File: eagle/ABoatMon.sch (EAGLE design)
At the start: 29 parts, among them J1 5V, J2 GND, J3 GND, J4 5V, X1 MKDSN1,5/2-5,08

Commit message: added M0
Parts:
- removed C1: 0.1U, SparkFun-Capacitors:0.1UF-KIT-EZ-50V-20%
- removed J4: 5V, SparkFun-Connectors:CONN_01
- removed JST1: LIPO, adafruit:JST_2PIN-THM
- removed LIPO: (no value), microbuilder:HEADER-1X2ROUND
- removed MOTEINO_MEGA: HEADERS, Moteino:MOTEINO_MEGA_SIMPLE
- removed R2: 1.8M, SparkFun-Resistors:1KOHM-HORIZ-1/4W-1%
- removed R3: 3.3M, SparkFun-Resistors:1KOHM-HORIZ-1/4W-1%
- added U$6: MOTEINO_M0, Moteino:MOTEINO_M0
- J1: value 5V -> VUSB
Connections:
- removed net 5V: J1.1, J4.1
- removed net A0: C1.1, MOTEINO_MEGA.A0, R2.1, R3.2
- removed net A5_VCC_VD: C2.1, MOTEINO_MEGA.A5, R5.2, R6.1
- removed net D10_GPS_RX: JP1.5, MOTEINO_MEGA.D10_RX1
- removed net D11_GPS_TX: JP1.4, MOTEINO_MEGA.D11_TX1
- removed net D12_GPS_ENABLE: JP1.8, MOTEINO_MEGA.D12
- removed net D13_FONA_NETSTAT: FONA.2, MOTEINO_MEGA.D13
- removed net D14_FONA_KEY: FONA.6, MOTEINO_MEGA.D14
- removed net D18_FONA_PS: FONA.7, MOTEINO_MEGA.D18
- removed net D19_PWRON: ENABLE.1, MOTEINO_MEGA.D19
- removed net D25_LED_SWITCH: JST.6, MOTEINO_MEGA.A1
- removed net D26_LED: MOTEINO_MEGA.A2, R7.2
- removed net D27_DS_PWR: JST.3, MOTEINO_MEGA.A3, R1.1
- removed net D28_DS_DATA: JST.5, MOTEINO_MEGA.A4, R1.2
- removed net D8_FONA_TX: FONA.3, MOTEINO_MEGA.D8_RX0
- removed net D9_FONA_RX: FONA.4, MOTEINO_MEGA.D9_TX0
- removed net VIN: FONA.12, LIPO.1, MOTEINO_MEGA.VIN, MOTEINO_MEGA.VIN_2, R2.2
- removed net VIN_JUMPER: JST1.2, LIPO.2
- new net A1_VCC_VD: C2.1, R5.2, R6.1, U$6.A1
- new net D0_RX_GPS: JP1.5, U$6.D0_RX1
- new net D10_FONA_KEY: FONA.6, U$6.D10
- new net D11_FONA_PS: FONA.7, U$6.D11
- new net D12_PWRON: ENABLE.1, U$6.D12
- new net D1_TX_GPS: JP1.4, U$6.D1_TX1
- new net D30_TX_FONA: FONA.3, U$6.D30_TX
- new net D31_RX_FONA: FONA.4, U$6.D31_RX
- new net D4_LED: R7.2, U$6.D4
- new net D5_LED_SWITCH: JST.6, U$6.D5
- new net D6_DS_PWR: JST.3, R1.1, U$6.D6
- new net D7_DS_DATA: JST.5, R1.2, U$6.D7
- new net D8_FONA_NETSTAT: FONA.2, U$6.D8
- new net D9_GPS_ENABLE: JP1.8, U$6.D9_DIO0
- new net VUSB: FONA.12, J1.1, U$6.VUSB
- net 3.3V: now also U$6.3V3, U$6.3V3_2; no longer MOTEINO_MEGA.3V3, MOTEINO_MEGA.3V3_2
- net D3_BILGESW: now also U$6.D3; no longer MOTEINO_MEGA.D3
- net GND: now also U$6.GND, U$6.GND1, U$6.GND2; no longer C1.2, JST1.1, MOTEINO_MEGA.GND1, MOTEINO_MEGA.GND2, R3.1
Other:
- note removed: "LIPO Voltage Divider/ADC"
- moved on the sheet: JP1, R1

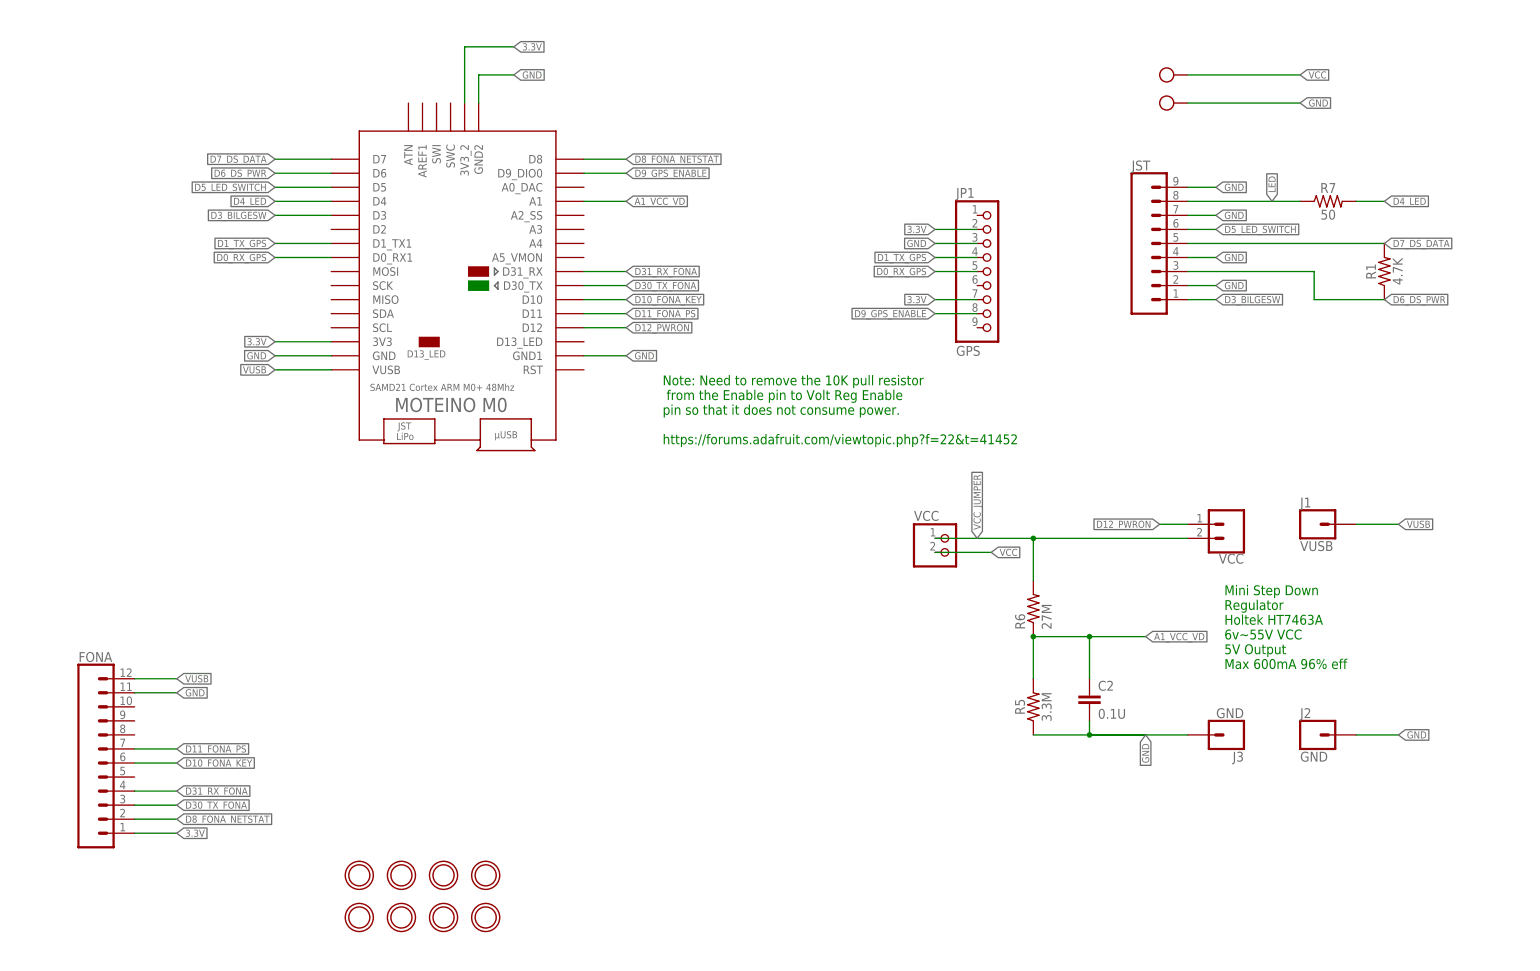
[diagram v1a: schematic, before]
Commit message: added CAM-M8
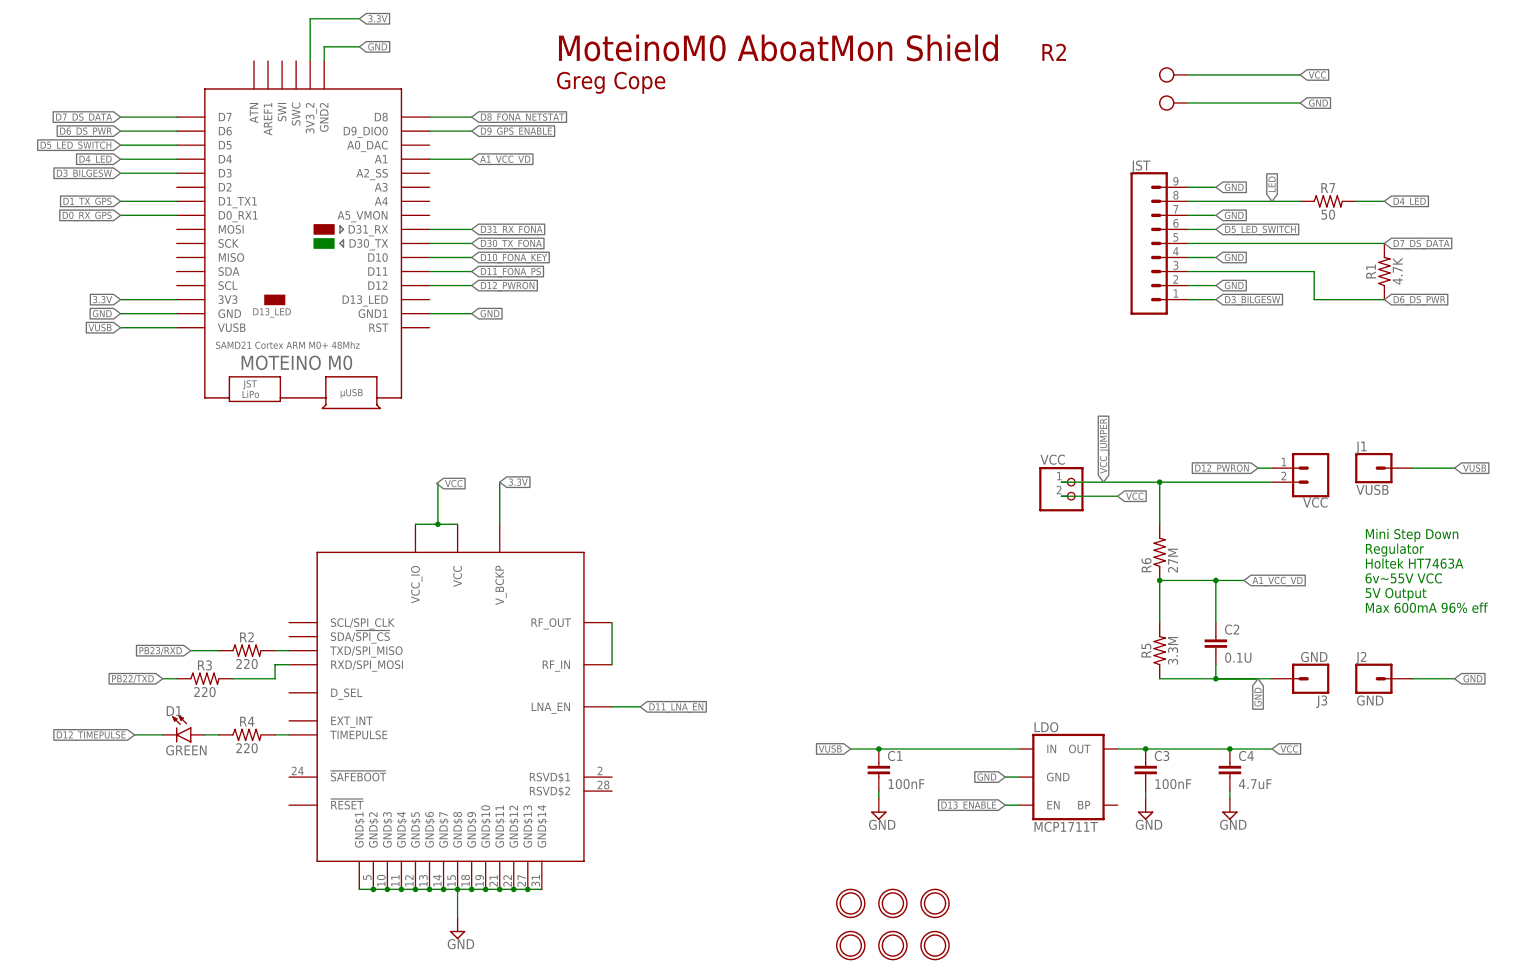
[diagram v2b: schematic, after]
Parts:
- removed FONA: (no value), SparkFun-Connectors:CONN_12
- removed JP1: GPS, microbuilder:HEADER-1X970MIL
- removed U$3: MOUNTINGHOLE2.5, microbuilder:MOUNTINGHOLE2.5
- added C1, C3: 100nF, SparkFun-Capacitors:0.1UF-0603-25V-5%
- added C4: 4.7uF, SparkFun-Capacitors:4.7UF0603
- added D1: GREEN, SparkFun-LED:LED-GREEN0603
- added LDO: MCP1711T, SparkFun-IC-Power:V_REG_SPX3819-SOT23-5
- added R2, R3, R4: 220, SparkFun-Resistors:220OHM-0603-1/10W-1%
- U$5: value MOUNTINGHOLE2.5 -> CAM-M8; device microbuilder:MOUNTINGHOLE2.5 -> ubloxLib:CAM-M8
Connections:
- new net D11_LNA_EN: U$5.LNA_EN
- new net D12_TIMEPULSE: D1.C
- new net D13_ENABLE: LDO.EN
- new net N$1: R4.2, U$5.TIMEPULSE
- new net N$2: R2.2, U$5.TXD/SPI_MISO
- new net N$3: R3.2, U$5.RXD/SPI_MOSI
- new net N$4: D1.A, R4.1
- new net N$5: U$5.RF_IN, U$5.RF_OUT
- new net PB22/TXD: R3.1
- new net PB23/RXD: R2.1
- net 3.3V: now also U$5.V_BCKP; no longer FONA.1, JP1.2, JP1.7
- net D0_RX_GPS: no longer JP1.5
- net D10_FONA_KEY: no longer FONA.6
- net D11_FONA_PS: no longer FONA.7
- net D1_TX_GPS: no longer JP1.4
- net D30_TX_FONA: no longer FONA.3
- net D31_RX_FONA: no longer FONA.4
- net D8_FONA_NETSTAT: no longer FONA.2
- net D9_GPS_ENABLE: no longer JP1.8
- net GND: now also C1.2, C3.2, C4.2, LDO.GND, U$5.GND$1, U$5.GND$10, U$5.GND$11, U$5.GND$12, U$5.GND$13, U$5.GND$14, U$5.GND$2, U$5.GND$3, U$5.GND$4, U$5.GND$5, U$5.GND$6, U$5.GND$7, U$5.GND$8, U$5.GND$9; no longer FONA.11, JP1.3
- net VCC: now also C3.1, C4.1, LDO.OUT, U$5.VCC, U$5.VCC_IO
- net VUSB: now also C1.1, LDO.IN; no longer FONA.12
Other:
- note added: "Greg Cope"
- note added: "MoteinoM0 AboatMon Shield"
- note added: "R2"
- note removed: "Note: Need to remove the 10K pull resistor from the Enable pin to Volt Reg Enable pin so that it does not consume power. https://forums.adafruit.com/viewtopic.php?f=22&t=41452"
- moved on the sheet: C2, J1, J2, J3, R5, R6, VCC
